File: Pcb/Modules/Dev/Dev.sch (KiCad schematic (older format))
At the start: 9 parts, among them J1 JACK_STEREO, J2 JACK_RJ45, P1 CONN_02X04, P2 CONN_02X04, Q1 BSS138P, U1 11AA160, X1 HOLE, X2 HOLE

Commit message: Update module pcbs to common format and fix issues.
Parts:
- removed Q1: BSS138P, CA6:SOT23, symbol BSS138P
- removed U1: 11AA160, CA6:SOT-23_11AA160, symbol 11AA160
- removed X1, X2: HOLE, CA6:HOLE_3.0mm, symbol HOLE
- added L1, L2: Ferrite_Bead, Resistors_SMD:R_0805, symbol Ferrite_Bead
- added Q1: Q_NMOS_GSD, TO_SOT_Packages_SMD:SOT-23, symbol Q_NMOS_GSD
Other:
- moved on the sheet: C1
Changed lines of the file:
@@
 LIBS:valves
 LIBS:CA6
+LIBS:Dev-cache
 EELAYER 25 0
 EELAYER END
@@
 $EndDescr
 $Comp
-L HOLE X1
-U 1 1 58C3153C
-P 850 900
-F 0 "X1" H 850 800 60  0000 C CNN
-F 1 "HOLE" H 850 1000 60  0000 C CNN
-F 2 "CA6:HOLE_3.0mm" H 850 900 60  0001 C CNN
-F 3 "" H 850 900 60  0000 C CNN
-	1    850  900
-	1    0    0    -1
-$EndComp
-$Comp
-L HOLE X2
-U 1 1 58C3160A
-P 1150 900
-F 0 "X2" H 1150 800 60  0000 C CNN
-F 1 "HOLE" H 1150 1000 60  0000 C CNN
-F 2 "CA6:HOLE_3.0mm" H 1150 900 60  0001 C CNN
-F 3 "" H 1150 900 60  0000 C CNN
-	1    1150 900
-	1    0    0    -1
-$EndComp
-$Comp
 L JACK_RJ45 J2
 U 1 1 58C31719
@@
 $EndComp
 $Comp
-L 3V3 #PWR01
+L 3V3 #PWR4
 U 1 1 58C31841
-P 2150 1250
-F 0 "#PWR01" H 2150 1350 40  0001 C CNN
-F 1 "3V3" H 2150 1375 40  0000 C CNN
-F 2 "" H 2150 1250 60  0000 C CNN
-F 3 "" H 2150 1250 60  0000 C CNN
-	1    2150 1250
+P 2500 1150
+F 0 "#PWR4" H 2500 1250 40  0001 C CNN
+F 1 "3V3" H 2500 1275 40  0000 C CNN
+F 2 "" H 2500 1150 60  0000 C CNN
+F 3 "" H 2500 1150 60  0000 C CNN
+	1    2500 1150
 	1    0    0    -1
 $EndComp
@@
 L C C1
 U 1 1 58C3185F
-P 2300 1400
-F 0 "C1" H 2325 1500 50  0000 L CNN
-F 1 "C" H 2325 1300 50  0001 L CNN
-F 2 "CA6:c_1206" H 2400 1300 50  0001 C CNN
-F 3 "" H 2300 1400 50  0000 C CNN
-	1    2300 1400
-	1    0    0    -1
-$EndComp
-$Comp
-L GND #PWR02
+P 2650 1400
+F 0 "C1" H 2675 1500 50  0000 L CNN
+F 1 "C" H 2675 1300 50  0001 L CNN
+F 2 "CA6:c_1206" H 2750 1300 50  0001 C CNN
+F 3 "" H 2650 1400 50  0000 C CNN
+	1    2650 1400
+	1    0    0    -1
+$EndComp
+$Comp
+L GND #PWR6
 U 1 1 58C3198F
-P 2300 1600
-F 0 "#PWR02" H 2300 1350 50  0001 C CNN
-F 1 "GND" H 2300 1450 50  0000 C CNN
-F 2 "" H 2300 1600 50  0000 C CNN
-F 3 "" H 2300 1600 50  0000 C CNN
-	1    2300 1600
-	1    0    0    -1
-$EndComp
-$Comp
-L GND #PWR03
+P 2650 1650
+F 0 "#PWR6" H 2650 1400 50  0001 C CNN
+F 1 "GND" H 2650 1500 50  0000 C CNN
+F 2 "" H 2650 1650 50  0000 C CNN
+F 3 "" H 2650 1650 50  0000 C CNN
+	1    2650 1650
+	1    0    0    -1
+$EndComp
+$Comp
+L GND #PWR5
 U 1 1 58C31B87
-P 1700 1950
-F 0 "#PWR03" H 1700 1700 50  0001 C CNN
-F 1 "GND" H 1700 1800 50  0000 C CNN
-F 2 "" H 1700 1950 50  0000 C CNN
-F 3 "" H 1700 1950 50  0000 C CNN
-	1    1700 1950
+P 2500 2050
+F 0 "#PWR5" H 2500 1800 50  0001 C CNN
+F 1 "GND" H 2500 1900 50  0000 C CNN
+F 2 "" H 2500 2050 50  0000 C CNN
+F 3 "" H 2500 2050 50  0000 C CNN
+	1    2500 2050
 	1    0    0    -1
 $EndComp
@@
 	1600 1550 1950 1550
 Wire Wire Line
-	1600 1650 2150 1650
+	1600 1650 1950 1650
 Wire Wire Line
 	1600 1750 1950 1750
@@
 	1600 1850 1950 1850
 Wire Wire Line
-	1600 1950 1700 1950
-Wire Wire Line
-	1600 1250 2300 1250
-Connection ~ 2150 1250
+	1600 1950 2000 1950
 Text Label 1950 1350 2    60   ~ 0
 A0
@@
 Text Label 1950 1850 2    60   ~ 0
 D4
-Wire Wire Line
-	2300 1550 2300 1600
-$Comp
-L 11AA160 U1
-U 1 1 58C3229B
-P 2800 2350
-F 0 "U1" H 2800 2500 50  0000 C CNN
-F 1 "11AA160" H 2800 2150 50  0000 C CNN
-F 2 "CA6:SOT-23_11AA160" H 2800 2350 50  0001 C CNN
-F 3 "DOCUMENTATION" H 2800 2350 50  0001 C CNN
-	1    2800 2350
-	1    0    0    -1
-$EndComp
 $Comp
 L JACK_STEREO J1
@@
 $EndComp
 $Comp
-L BSS138P Q1
-U 1 1 58C32499
-P 1950 3000
-F 0 "Q1" H 1850 2750 60  0000 C CNN
-F 1 "BSS138P" H 1700 3250 60  0000 C CNN
-F 2 "CA6:SOT23" H 1800 3050 60  0001 C CNN
-F 3 "" H 1800 3050 60  0000 C CNN
-	1    1950 3000
-	-1   0    0    -1
-$EndComp
-$Comp
 L CONN_02X04 P1
 U 1 1 58C324F0
@@
 	1400 2700 1950 2700
 $Comp
-L GND #PWR04
+L GND #PWR2
 U 1 1 58C329B9
 P 1950 3350
-F 0 "#PWR04" H 1950 3100 50  0001 C CNN
+F 0 "#PWR2" H 1950 3100 50  0001 C CNN
 F 1 "GND" H 1950 3200 50  0000 C CNN
 F 2 "" H 1950 3350 50  0000 C CNN
@@
 A0
 $Comp
-L GND #PWR05
+L GND #PWR1
 U 1 1 58C32A9C
 P 1500 3000
-F 0 "#PWR05" H 1500 2750 50  0001 C CNN
+F 0 "#PWR1" H 1500 2750 50  0001 C CNN
 F 1 "GND" H 1500 2850 50  0000 C CNN
 F 2 "" H 1500 3000 50  0000 C CNN
@@
 $EndComp
 Wire Wire Line
-	1950 3300 1950 3350
+	1950 3200 1950 3350
 Wire Wire Line
 	1400 3000 1500 3000
@@
 Text Label 2500 3000 2    60   ~ 0
 D1
-Wire Wire Line
-	2200 2250 2150 2250
-Wire Wire Line
-	2150 2250 2150 1650
-$Comp
-L 3V3 #PWR06
-U 1 1 58C33907
-P 2050 2400
-F 0 "#PWR06" H 2050 2500 40  0001 C CNN
-F 1 "3V3" H 2050 2525 40  0000 C CNN
-F 2 "" H 2050 2400 60  0000 C CNN
-F 3 "" H 2050 2400 60  0000 C CNN
-	1    2050 2400
-	1    0    0    -1
-$EndComp
-Wire Wire Line
-	2200 2450 2050 2450
-Wire Wire Line
-	2050 2450 2050 2400
-$Comp
-L GND #PWR07
-U 1 1 58C3394E
-P 3500 2350
-F 0 "#PWR07" H 3500 2100 50  0001 C CNN
-F 1 "GND" H 3500 2200 50  0000 C CNN
-F 2 "" H 3500 2350 50  0000 C CNN
-F 3 "" H 3500 2350 50  0000 C CNN
-	1    3500 2350
-	1    0    0    -1
-$EndComp
-Wire Wire Line
-	3500 2350 3400 2350
 $Comp
 L CONN_02X04 P2
@@
 NoConn ~ 2950 200
 $Comp
-L GND #PWR08
+L GND #PWR8
 U 1 1 58C34106
 P 3800 3400
-F 0 "#PWR08" H 3800 3150 50  0001 C CNN
+F 0 "#PWR8" H 3800 3150 50  0001 C CNN
 F 1 "GND" H 3800 3250 50  0000 C CNN
 F 2 "" H 3800 3400 50  0000 C CNN
@@
 $EndComp
 $Comp
-L 3V3 #PWR09
+L 3V3 #PWR9
 U 1 1 58C3412C
 P 4850 3400
-F 0 "#PWR09" H 4850 3500 40  0001 C CNN
+F 0 "#PWR9" H 4850 3500 40  0001 C CNN
 F 1 "3V3" H 4850 3525 40  0000 C CNN
 F 2 "" H 4850 3400 60  0000 C CNN
@@
 D4
 $Comp
-L GND #PWR?
+L GND #PWR3
 U 1 1 58C35D47
 P 2400 3400
-F 0 "#PWR?" H 2400 3150 50  0001 C CNN
+F 0 "#PWR3" H 2400 3150 50  0001 C CNN
 F 1 "GND" H 2400 3250 50  0000 C CNN
 F 2 "" H 2400 3400 50  0000 C CNN
@@
 $EndComp
 $Comp
-L 3V3 #PWR?
+L 3V3 #PWR7
 U 1 1 58C35D6D
 P 3150 3400
-F 0 "#PWR?" H 3150 3500 40  0001 C CNN
+F 0 "#PWR7" H 3150 3500 40  0001 C CNN
 F 1 "3V3" H 3150 3525 40  0000 C CNN
 F 2 "" H 3150 3400 60  0000 C CNN
@@
 Wire Wire Line
 	3050 3400 3150 3400
+$Comp
+L Ferrite_Bead L1
+U 1 1 59C1AAE6
+P 2100 1250
+F 0 "L1" V 1950 1275 50  0000 C CNN
+F 1 "Ferrite_Bead" V 2250 1250 50  0001 C CNN
+F 2 "Resistors_SMD:R_0805" V 2030 1250 50  0001 C CNN
+F 3 "" H 2100 1250 50  0000 C CNN
+	1    2100 1250
+	0    1    1    0
+$EndComp
+$Comp
+L Ferrite_Bead L2
+U 1 1 59C1ADF6
+P 2150 1950
+F 0 "L2" V 2000 1975 50  0000 C CNN
+F 1 "Ferrite_Bead" V 2300 1950 50  0001 C CNN
+F 2 "Resistors_SMD:R_0805" V 2080 1950 50  0001 C CNN
+F 3 "" H 2150 1950 50  0000 C CNN
+	1    2150 1950
+	0    -1   -1   0
+$EndComp
+Wire Wire Line
+	1950 1250 1600 1250
+Wire Wire Line
+	2250 1250 2650 1250
+Wire Wire Line
+	2500 1150 2500 1250
+Connection ~ 2500 1250
+Wire Wire Line
+	2650 1550 2650 1650
+Wire Wire Line
+	2300 1950 2500 1950
+Wire Wire Line
+	2500 1950 2500 2050
+$Comp
+L Q_NMOS_GSD Q1
+U 1 1 59C1B522
+P 2050 3000
+F 0 "Q1" H 2250 3050 50  0000 L CNN
+F 1 "Q_NMOS_GSD" H 2250 2950 50  0001 L CNN
+F 2 "TO_SOT_Packages_SMD:SOT-23" H 2250 3100 50  0001 C CNN
+F 3 "" H 2050 3000 50  0000 C CNN
+	1    2050 3000
+	-1   0    0    -1
+$EndComp
+Wire Wire Line
+	1950 2700 1950 2800
 $EndSCHEMATC

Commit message: Update dev module pcb
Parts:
- removed L1, L2: Ferrite_Bead, Resistors_SMD:R_0805, symbol Ferrite_Bead
- removed P2: CONN_02X04, Socket_Strips:Socket_Strip_Straight_2x04_Pitch2.54mm, symbol CONN_02X04
- added SW0: SW_TACTILE, CA6:PTS645, symbol SW_TACTILE
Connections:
- net 3V3: now also J2.1
- net GND: now also J2.8, SW0.1, SW0.2
- net A0 renamed M_0
- net D1 renamed M_1
- net D2 renamed M_2
- net M_2: now also SW0.3, SW0.4
- net D3 renamed M_4
- net D4 renamed M_5
- net ID renamed M_3
- no-connect marks 7 -> 1
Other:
- moved on the sheet: P1, Q1

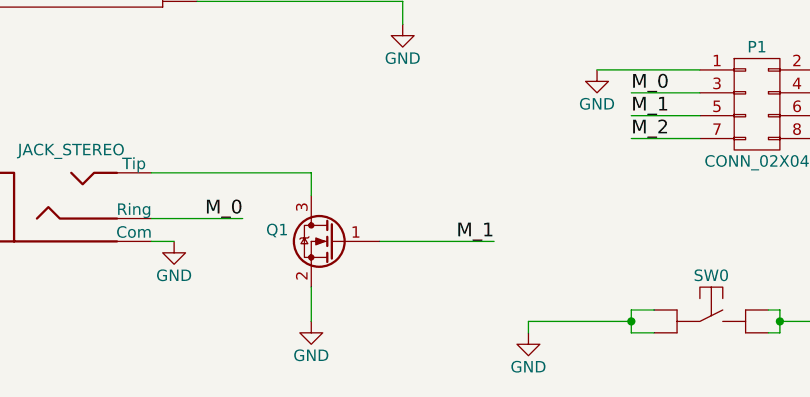
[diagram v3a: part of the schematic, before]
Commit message: Fix some issues with dev module and cleanup light module
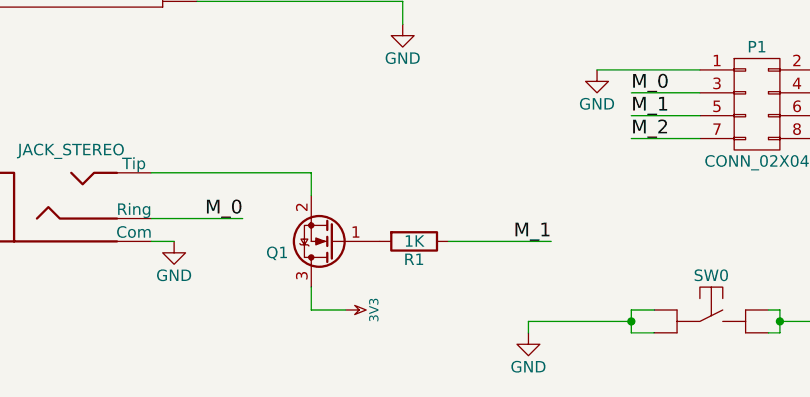
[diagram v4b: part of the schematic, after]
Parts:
- added R1: 1K, symbol R
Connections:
- net 3V3: now also Q1.3 (D)
- net GND: no longer Q1.2 (S)
- net M_1: now also R1.1; no longer Q1.1 (G)
- net at J1.2 (Tip): now also Q1.2 (S); no longer Q1.3 (D)
- new net: Q1.1 (G), R1.2
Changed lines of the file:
@@
 Wire Wire Line
 	1400 2700 2100 2700
-$Comp
-L GND #PWR2
-U 1 1 58C329B9
-P 2100 3350
-F 0 "#PWR2" H 2100 3100 50  0001 C CNN
-F 1 "GND" H 2100 3200 50  0000 C CNN
-F 2 "" H 2100 3350 50  0000 C CNN
-F 3 "" H 2100 3350 50  0000 C CNN
-	1    2100 3350
-	1    0    0    -1
-$EndComp
 Wire Wire Line
 	1400 2900 1800 2900
@@
 	1    0    0    -1
 $EndComp
-Wire Wire Line
-	2100 3200 2100 3350
 Wire Wire Line
 	1400 3000 1500 3000
@@
 F 3 "" H 2200 3000 50  0000 C CNN
 	1    2200 3000
-	-1   0    0    -1
+	-1   0    0    1
 $EndComp
-Wire Wire Line
-	2100 2700 2100 2800
 $Comp
 L SW_TACTILE SW0
@@
 Connection ~ 4150 3350
 Wire Wire Line
-	2400 3000 2900 3000
+	2700 3000 3150 3000
 Wire Wire Line
 	3500 3300 3500 3400
@@
 	3500 3350 3050 3350
 Connection ~ 3500 3350
-Text Label 2900 3000 2    60   ~ 0
+Text Label 3150 3000 2    60   ~ 0
 M_1
 $Comp
@@
 	1    0    0    -1
 $EndComp
+$Comp
+L R R1
+U 1 1 59E3F630
+P 2550 3000
+F 0 "R1" V 2630 3000 50  0000 C CNN
+F 1 "1K" V 2550 3000 50  0000 C CNN
+F 2 "" V 2480 3000 50  0000 C CNN
+F 3 "" H 2550 3000 50  0000 C CNN
+	1    2550 3000
+	0    1    1    0
+$EndComp
+$Comp
+L 3V3 #PWR?
+U 1 1 59E3F80E
+P 2250 3300
+F 0 "#PWR?" H 2250 3400 40  0001 C CNN
+F 1 "3V3" H 2250 3425 40  0000 C CNN
+F 2 "" H 2250 3300 60  0000 C CNN
+F 3 "" H 2250 3300 60  0000 C CNN
+	1    2250 3300
+	0    1    1    0
+$EndComp
+Wire Wire Line
+	2250 3300 2100 3300
+Wire Wire Line
+	2100 3300 2100 3200
+Wire Wire Line
+	2100 2700 2100 2800
 $EndSCHEMATC
